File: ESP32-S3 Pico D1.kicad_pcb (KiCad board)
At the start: 6 copper layers, 31 x 30.5 mm, 88 parts, among them CN1 GT-USB-7014D, CN2 BM04B-ACHSS, CN3 2337019-1, SW1 SPST-NO, SW2 SPST-NO, U1 SKYA21024, U11 74LVC1G38, U12 74LVC1G38, U13 74LVC1G38, U2 TPS2121, U3 TPS2121, U4 TPSM82903, U5 TPSM82903, U6 ESP32-S3-PICO-1-N8R2, U8 TCAN1057AVDRBRQ1, U9 TS3USB221A-Q1

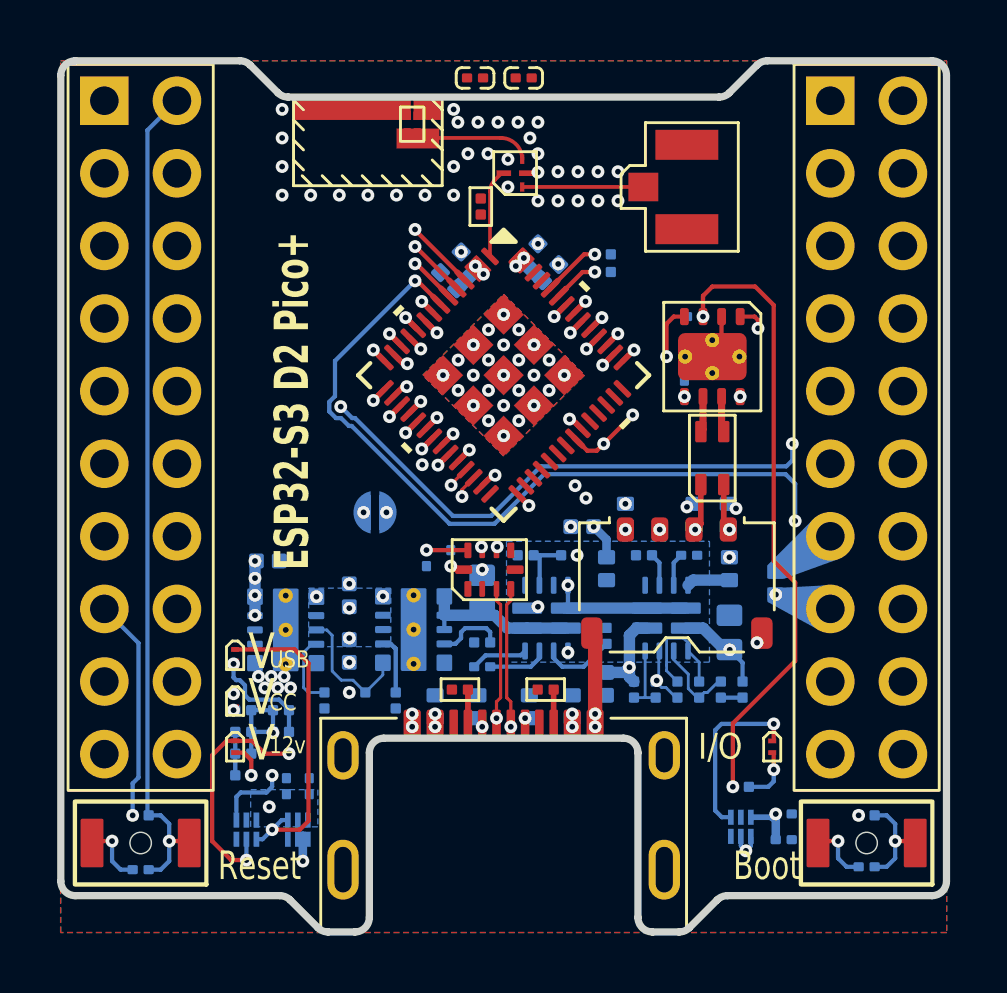
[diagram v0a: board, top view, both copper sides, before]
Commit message: streamlined routing by discarding legacy GPIO pinout compatibility. reduced Vin to Vcc and Vbus (no more +16V) includes CAN & Vehicle inputs (need to move to 2nd board, though) added wake-on-start by wiring Vacc to RTC_IO
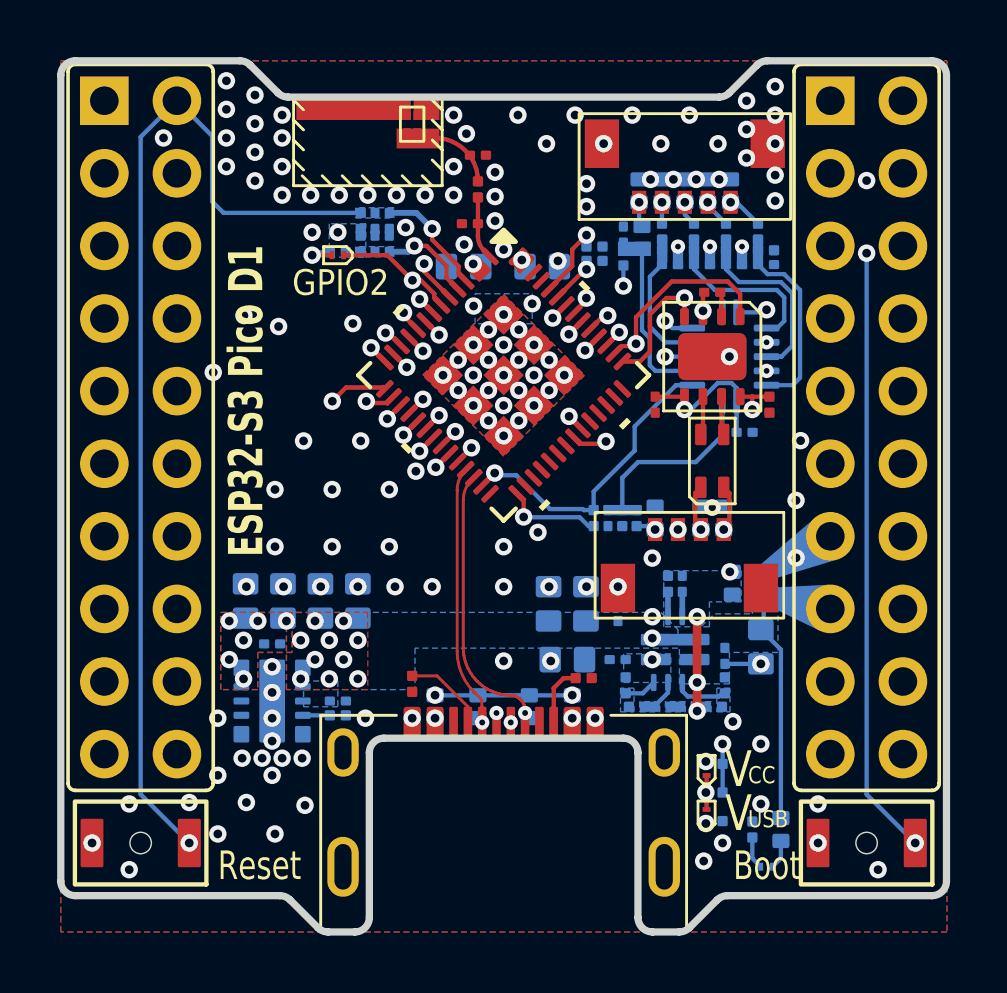
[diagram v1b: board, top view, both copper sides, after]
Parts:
- removed JP1: SolderJumper_2_Open, Personal_FootprintLibrary:SolderJumper-2_Open
- removed R22: 1k, Resistors:R0201_Dense
- removed U11, U12, U13: 74LVC1G38, Personal_FootprintLibrary:DSF6
- removed U6: ESP32-S3-PICO-1-N8R2, Personal_FootprintLibrary:ESP32-S3-Pico-1
- removed U8: TCAN1057AVDRBRQ1, Personal_FootprintLibrary:VSON-8-1EP_3x3mm_P0.65mm_EP1.65x2.4mm_ThermalVias
- removed U9: TS3USB221A-Q1, Personal_FootprintLibrary:Texas_UQFN-10_1.5x2mm_P0.5mm
- added C13: 47uF, Capacitors:C_0603_Dense, B.Cu at (142.3, 118.9)
- added C27: 1uF, Capacitors:C_0201_Dense, B.Cu at (159.2, 107.1)
- added C30: 1uF, Capacitors:C_0201_Dense, B.Cu at (155.8, 107.1)
- added C31: 1uF, Capacitors:C_0201_Dense, B.Cu at (153.7, 116.0)
- added C32: 1uF, Capacitors:C_0201_Dense, B.Cu at (154.2, 106.1)
- added C7: 1uF, Capacitors:C_0201_Dense, B.Cu at (144.2, 122.4)
- added D11: D15V0H1U2LP-7B, Personal_FootprintLibrary:DFN1006-2, B.Cu at (157.9, 104.5)
- added D12: D15V0H1U2LP-7B, Personal_FootprintLibrary:DFN1006-2, B.Cu at (157.1, 104.5)
- added D13: D15V0H1U2LP-7B, Personal_FootprintLibrary:DFN1006-2, B.Cu at (156.3, 104.5)
- added D14: D15V0H1U2LP-7B, Personal_FootprintLibrary:DFN1006-2, B.Cu at (155.5, 104.5)
- added D15: D15V0H1U2LP-7B, Personal_FootprintLibrary:DFN1006-2, B.Cu at (154.7, 104.5)
- added D16: D15V0H1U2LP-7B, Personal_FootprintLibrary:DFN1006-2, B.Cu at (154.8, 106.2)
- added R25: 10k, Resistors:R_0201_Dense, B.Cu at (159.2, 106.6)
- added R29: 10k, Resistors:R_0201_Dense, B.Cu at (156.9, 106.6)
- added R31: 10k, Resistors:R_0201_Dense, B.Cu at (155.8, 106.6)
- added R32: 26k1, Resistors:R_0201_Dense, B.Cu at (154.2, 116.0)
- added R33: 10k, Resistors:R_0201_Dense, B.Cu at (153.2, 116.0)
- added R35: 10k, Resistors:R_0201_Dense, B.Cu at (154.2, 106.9)
- C1: value 22uF -> 47uF; footprint Capacitors:C0603_Dense -> Capacitors:C_0603_Dense
- C10, C12, C19, C2, C20, C21, C3: value 22uF -> 1uF; footprint Capacitors:C0402_Dense -> Capacitors:C_0201_Dense
- C11: value 22uF -> 47uF; footprint Capacitors:C0402_Dense -> Capacitors:C_0603_Dense
- C14, C23, C4, C5, C8, C9: value 1uF -> 47uF; footprint Capacitors:C0201_Dense -> Capacitors:C_0603_Dense
- C15, C16: value 1uF -> DNP; footprint Capacitors:C0201_Dense -> Capacitors:C_0201_Dense; moved to F.Cu
- C17: value 22uF -> 1uF; footprint Capacitors:C0402_Dense -> Capacitors:C_0201_Dense; moved to F.Cu
- C18: value 22uF -> 1uF; footprint Capacitors:C0603_Dense -> Capacitors:C_0201_Dense; moved to F.Cu
- C22: value 100nF -> 1uF; footprint Capacitors:C0201_Dense -> Capacitors:C_0201_Dense
- C24: value 100nF -> 47uF; footprint Capacitors:C0201_Dense -> Capacitors:C_0603_Dense
- C26, C6: footprint Capacitors:C0201_Dense -> Capacitors:C_0201_Dense
- C28, C29: value DNP -> 1uF; footprint Capacitors:C0201_Dense -> Capacitors:C_0201_Dense; moved to B.Cu
- CN2: value BM04B-ACHSS -> SM04B-SURS-TF(LF)(SN); footprint Personal_FootprintLibrary:JST_ACH_BM04B-ACHSS-A-GAN-ETF_1x04-1MP_P1.20mm_Vertical -> Personal_FootprintLibrary:JST_SUH_1x04_MP_P0.8mm
- CN3: value 2337019-1 -> SM05B-SURS-TF(LF)(SN); footprint Personal_FootprintLibrary:u.FL_Male_Pin_Coax_SMD -> Personal_FootprintLibrary:JST_SUH_1x05_MP_P0.8mm
- D2: value ESDSLC24VLB-TP -> D15V0H1U2LP-7B
- D3, D7, D8: value ESDSLC24VLB-TP -> SZESD7241N2T5G
- D4: value D15V0H1U2LP-7B -> SZESD7241N2T5G
- H1, H2: footprint Personal_FootprintLibrary:PinHeader_2x10_P2.54mm_Vertical -> Personal_FootprintLibrary:PinHeader_2x10_P2.54mm_Vertical_BottomMount_TopReference
- LED2: value Green -> Orange
- LED3: value Orange -> Green
- LED4: moved to B.Cu
- R1: value 40k2 -> 5k1; footprint Resistors:R0201_Dense -> Resistors:R_0201_Dense; moved to F.Cu
- R10: value 1k -> 5k1; footprint Resistors:R0201_Dense -> Resistors:R_0201_Dense
- R11: value 1k -> 0R; footprint Resistors:R0201_Dense -> Resistors:R_0201_Dense; moved to F.Cu
- R12, R13, R19, R23: footprint Resistors:R0201_Dense -> Resistors:R_0201_Dense
- R14, R16, R17: value 95k3 -> 5k1; footprint Resistors:R0201_Dense -> Resistors:R_0201_Dense
- R15, R9: value 40k2 -> 5k1; footprint Resistors:R0201_Dense -> Resistors:R_0201_Dense
- R18: value 40k2 -> 1k; footprint Resistors:R0201_Dense -> Resistors:R_0201_Dense
- R2: value 95k3 -> 5k1; footprint Resistors:R0201_Dense -> Resistors:R_0201_Dense; moved to F.Cu
- R20: footprint Resistors:R0201_Dense -> Resistors:R_0201_Dense; moved to F.Cu
- R21, R4, R7: value 95k3 -> 76k8; footprint Resistors:R0201_Dense -> Resistors:R_0201_Dense
- R24: value 1k -> 47k; footprint Resistors:R0201_Dense -> Resistors:R_0201_Dense
- R26: value 95k3 -> 47k; footprint Resistors:R0201_Dense -> Resistors:R_0201_Dense
- R27: value 40k2 -> 10k; footprint Resistors:R0201_Dense -> Resistors:R_0201_Dense
- R28: value 40k2 -> 47k; footprint Resistors:R0201_Dense -> Resistors:R_0201_Dense
- R3: value 40k2 -> 76k8; footprint Resistors:R0201_Dense -> Resistors:R_0201_Dense
- R30: value 0R -> 47k; footprint Resistors:R0201_Dense -> Resistors:R_0201_Dense; moved to B.Cu
- R5: value 5k1 -> 26k1; footprint Resistors:R0201_Dense -> Resistors:R_0201_Dense; moved to B.Cu
- R6: value 5k1 -> 76k8; footprint Resistors:R0201_Dense -> Resistors:R_0201_Dense; moved to B.Cu
- R8: value 1k -> 26k1; footprint Resistors:R0201_Dense -> Resistors:R_0201_Dense
- U1: value SKYA21024 -> TPS2121; footprint Personal_FootprintLibrary:SKYA21024 -> Personal_FootprintLibrary:VQHN-HR-12; moved to B.Cu
- U2: value TPS2121 -> TPSM82903; footprint Personal_FootprintLibrary:VQHN-HR-12 -> Personal_FootprintLibrary:uSIP-11_3.0x2.8
- U3: value TPS2121 -> ESP32-S3-PICO-1-N8R2; footprint Personal_FootprintLibrary:VQHN-HR-12 -> Personal_FootprintLibrary:ESP32-S3-Pico-1; moved to F.Cu
- U4: value TPSM82903 -> TCAN1057AVDRBRQ1; footprint Personal_FootprintLibrary:uSIP-11_3.0x2.8_ThermalVias -> Personal_FootprintLibrary:VSON-8-1EP_3x3mm_P0.65mm_EP1.65x2.4mm; moved to F.Cu
- U5: value TPSM82903 -> 74LVC06A; footprint Personal_FootprintLibrary:uSIP-11_3.0x2.8_ThermalVias -> Personal_FootprintLibrary:DHVQFN-14-1EP_2.5x3mm_P0.5mm_EP1x1.5mm
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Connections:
- ANT1 pad 1: /ESP32-S3-PICO-1/RF2 -> /ESP32-S3-PICO-1/RF_Feed
- ANT1 pad 4: /ESP32-S3-PICO-1/RF2 -> /ESP32-S3-PICO-1/RF_Feed
- C1 pad 1: 2121b -> +VBus
- C11 pad 1: +3V3 -> +5VF
- C12 pad 1: +3V3 -> +5Vext
- C15 pad 1: OV1a -> /ESP32-S3-PICO-1/RF_In
- C16 pad 1: /USB_Power_Interface/SSa -> /ESP32-S3-PICO-1/RF_Feed
- C16 pad 2: /USB_Power_Interface/GND1 -> GND
- C17 pad 1: +3V3 -> +5VF
- C18 pad 1: +16V -> +3V3
- C19 pad 1: +3V3 -> EN
- C2 pad 1: +5V1 -> +VBus
- C20 pad 1: +5Vext -> EN
- C21 pad 1: +VBus -> IO_00
- C22 pad 1: +3V3 -> IO_00
- C28 pad 1: /ESP32-S3-PICO-1/RF_In -> /CAN_Interface/Brake_F
- C29 pad 1: /ESP32-S3-PICO-1/RFC -> /CAN_Interface/Right_F
- C3 pad 1: +5V1 -> /USB_Power_Interface/SS
- C3 pad 2: GND -> GND1
- C4 pad 1: +5V1 -> +5Vext
- C5 pad 1: +3V3 -> +5VF
- C6 pad 1: /USB_Power_Interface/SSb -> +5VF
- C6 pad 2: /USB_Power_Interface/GND1 -> GND
- C8 pad 1: EN -> +5VF
- C9 pad 1: IO_00 -> +5VF
- CN2 pad 1: +16V -> /CAN_Interface/Vacc
- CN3 pad 1: /ESP32-S3-PICO-1/RF1 -> /CAN_Interface/Reverse
- CN3 pad 2: GND -> /CAN_Interface/Brake
- D10 pad 1: +VBus -> +5Vext
- D10 pad 2: GND -> /User Interface/LED4_L
- D2 pad 1: USB_D+ -> +VBus
- D3 pad 1: USB_D- -> USB_D+
- D4 pad 1: GND -> USB_D-
- D4 pad 2: /USB_Power_Interface/GND1 -> GND
- D6 pad 2: /USB_Power_Interface/GND1 -> GND1
- D9 pad 1: +16V -> /CAN_Interface/Vacc
- H1 pad 10: IO_10 -> IO_11
- H1 pad 17: IO_11 -> IO_13
- H1 pad 19: IO_13 -> IO_12
- H1 pad 20: IO_12 -> IO_10
- H1 pad 9: +5V1 -> +5VF
- H2 pad 1: unconnected-(H2-Pin_1-Pad1) -> IO_46
- H2 pad 16: IO_47 -> CAN_Silent
- H2 pad 19: IO_14 -> IO_21
- H2 pad 2: CAN_Silent -> IO_45
- H2 pad 9: IO_21 -> IO_14
- LED1 pad 1: /User Interface/LED1_L -> IO_02
- LED1 pad 2: /User Interface/LED1_H -> /User Interface/LED2_H
- LED2 pad 1: /User Interface/LED2_L -> ST
- LED2 pad 2: /User Interface/LED2_H -> /User Interface/LED1_H
- LED3 pad 2: /User Interface/LED3_H -> ST
- LED4 pad 1: STb -> /User Interface/LED4_L
- R1 pad 2: /USB_Power_Interface/SCONFc -> /USB_Power_Interface/CC2
- R10 pad 1: /User Interface/LED3_H -> GND1
- R10 pad 2: +5V1 -> /USB_Power_Interface/OV2
- R11 pad 1: /User Interface/LED4_SR -> /ESP32-S3-PICO-1/RF_In
- R11 pad 2: +5V1 -> /ESP32-S3-PICO-1/RF_Feed
- R12 pad 1: IO_00 -> GND
- R12 pad 2: +3V3 -> IO_46
- R13 pad 1: EN -> GND
- R13 pad 2: +3V3 -> IO_45
- R14 pad 1: GND -> ST
- R14 pad 2: CAN_Silent -> +3V3
- R15 pad 1: /USB_Power_Interface/GND1 -> /User Interface/LED1_H
- R15 pad 2: /USB_Power_Interface/ILMa -> +3V3
- R16 pad 1: +VBus -> EN
- R16 pad 2: /USB_Power_Interface/PR1a -> +3V3
- R17 pad 1: /USB_Power_Interface/PR1a -> IO_00
- R17 pad 2: OV1a -> +3V3
- R18 pad 1: Net-(R18-Pad1) -> /User Interface/LED2_H
- R18 pad 2: +16V -> +3V3
- R19 pad 1: /USB_Power_Interface/OV2a -> GND
- R19 pad 2: Net-(R18-Pad1) -> /User Interface/LED3_L
- R2 pad 1: /USB_Power_Interface/VSETc -> GND
- R2 pad 2: GND -> /USB_Power_Interface/CC1
- R20 pad 1: /USB_Power_Interface/GND1 -> GND
- R20 pad 2: /USB_Power_Interface/OV2a -> CAN_Silent
- R21 pad 1: OV1a -> /CAN_Interface/VaccF
- R21 pad 2: /USB_Power_Interface/GND1 -> /CAN_Interface/Vacc
- R23 pad 1: /User Interface/LED2_H -> GND
- R23 pad 2: +5V1 -> /User Interface/LED4_H
- R24 pad 1: /User Interface/LED4_H -> /CAN_Interface/Rev_F
- R24 pad 2: /User Interface/LED4_SR -> /CAN_Interface/Reverse
- R26 pad 1: +5Vext -> /CAN_Interface/Brake_F
- R26 pad 2: /USB_Power_Interface/OV2b -> /CAN_Interface/Brake
- R27 pad 1: /USB_Power_Interface/GND1 -> GND
- R27 pad 2: /USB_Power_Interface/ILMb -> /CAN_Interface/Brake_F
- R28 pad 1: /USB_Power_Interface/GND1 -> /CAN_Interface/Right_F
- R28 pad 2: /USB_Power_Interface/OV2b -> /CAN_Interface/R_Turn
- R3 pad 1: GND -> +VBus
- R3 pad 2: /USB_Power_Interface/SCONFd -> /USB_Power_Interface/PR1
- R30 pad 1: /ESP32-S3-PICO-1/RF_In -> /CAN_Interface/Left_F
- R30 pad 2: /ESP32-S3-PICO-1/RFC -> /CAN_Interface/L_Turn
- R4 pad 1: +5V1 -> /USB_Power_Interface/PR1
- R4 pad 2: /USB_Power_Interface/PG_EN -> /USB_Power_Interface/OV1
- R5 pad 1: GND -> GND1
- R5 pad 2: /USB_Power_Interface/CC2 -> /USB_Power_Interface/OV1_x
- R6 pad 1: GND -> +5Vext
- R6 pad 2: /USB_Power_Interface/CC1 -> /USB_Power_Interface/OV2
- R7 pad 1: GND -> /USB_Power_Interface/ILM
- R7 pad 2: /ESP32-S3-PICO-1/Ant_Select -> GND1
- R8 pad 1: /User Interface/LED1_H -> GND
- R8 pad 2: +5V1 -> /USB_Power_Interface/SCONFd
- R9 pad 1: /User Interface/LED2_H -> /USB_Power_Interface/OV1_x
- R9 pad 2: +5V1 -> /USB_Power_Interface/OV1
- U1 pad 1: +3V3 -> +5VF
- U1 pad 2: /ESP32-S3-PICO-1/RF1 -> +5Vext
- U1 pad 3: GND -> GND1
- U1 pad 4: /ESP32-S3-PICO-1/RF2 -> /USB_Power_Interface/OV2
- U1 pad 5: /ESP32-S3-PICO-1/Ant_Select -> /USB_Power_Interface/OV1
- U1 pad 6: /ESP32-S3-PICO-1/RFC -> /USB_Power_Interface/PR1
- U2 pad 1: 2121a -> +5VF
- U2 pad 10: /USB_Power_Interface/ILMa -> +3V3
- U2 pad 11: /USB_Power_Interface/SSa -> GND
- U2 pad 2: +16V -> +5VF
- U2 pad 3: /USB_Power_Interface/GND1 -> +5VF
- U2 pad 4: /USB_Power_Interface/OV2a -> /USB_Power_Interface/SCONFd
- U2 pad 5: OV1a -> unconnected-(U2-SS/TR-Pad5)
- U2 pad 6: /USB_Power_Interface/PR1a -> GND
- U2 pad 7: +VBus -> unconnected-(U2-FB/VSET-Pad7)
- U2 pad 8: 2121a -> unconnected-(U2-SW-Pad8)
- U2 pad 9: /USB_Power_Interface/GND1 -> +3V3
- U3 pad 1: 2121b -> /ESP32-S3-PICO-1/RF_In
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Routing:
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- added copper zone on F.Cu, net +3V3
- added copper zone on In2.Cu, net +3V3
- added copper zone on B.Cu, net +5VF
- added copper zone on F.Cu, net +5VF
- added copper zone on In1.Cu, net +5VF
- added copper zone on In2.Cu, net +5VF
- added copper zone on In3.Cu, net +5VF
- added copper zone on B.Cu, net +5Vext
- added copper zone on B.Cu, net +VBus
- added copper zone on In4.Cu, net +VBus
- added copper zone on B.Cu, net /USB_Power_Interface/OV1
- added copper zone on B.Cu, net /USB_Power_Interface/OV1_x
- added copper zone on B.Cu, net /USB_Power_Interface/OV2
- added copper zone on B.Cu, net /USB_Power_Interface/PR1
- added copper zone on B.Cu, net EN
- added copper zone on B.Cu, net GND1
- added copper zone on B.Cu, net IO_00
- removed copper zone on B.Cu, net +5V1
- removed copper zone on In4.Cu, net +5V1
- removed copper zone on B.Cu, net /USB_Power_Interface/GND1
- removed copper zone on In1.Cu, net /USB_Power_Interface/GND1
- removed copper zone on In2.Cu, net /USB_Power_Interface/GND1
- removed copper zone on In3.Cu, net /USB_Power_Interface/GND1
- removed copper zone on In4.Cu, net /USB_Power_Interface/GND1
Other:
- board text added: "ESP32-S3 Pico D1"
- board text added: "GPIO2"
- board text added: "Polarity!"
- board text added: "RHK ESP32-S3 D2 Pico"
- board text added: "Reverse"
- board text removed: "12v"
- board text removed: "ESP32-S3 D2 Pico+"
- board text removed: "I/O"
- board text removed: "RHK ESP32-S3 D2 Pico+"

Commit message: Update .gitignore, BOM-ESP32-S3 Pico D1.csv, CANBus_Interface.kicad_sch, and 14 more files
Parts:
- removed CN2: SM04B-SURS-TF(LF)(SN), Personal_FootprintLibrary:JST_SUH_1x04_MP_P0.8mm
- removed CN3: SM05B-SURS-TF(LF)(SN), Personal_FootprintLibrary:JST_SUH_1x05_MP_P0.8mm
- removed R23: 5k1, Resistors:R_0201_Dense
- added J**: BM20BNSHDZSTFT, 000JST:BM20BNSHDZSTFT, F.Cu at (145.6, 80.3)
- added J**: BM20BNSHDZSTFT, 000JST:BM20BNSHDZSTFT, F.Cu at (154.4, 80.3)
- added J**: SM10B-NSHSS-TB-LFSN, 000JST:SM10B-NSHSS-TB-LFSN, F.Cu at (150.0, 94.3)
- added OSC1: 40MHz, Personal_FootprintLibrary:SIT8XXXxx-7Y-xxx, F.Cu at (175.1, 120.8)
- added R22: 5k1, Resistors:R_0201_Dense, B.Cu at (157.4, 126.6)
- added REF**: SAMTEC_HLE-110-02-L-DV-BE-K-TR, Personal_FootprintLibrary:PinHeader_2x10_P2.54mm_LowProfile_BottomEntrySMD, F.Cu at (137.3, 86.0)
- added REF**: SAMTEC_HLE-110-02-L-DV-BE-K-TR, Personal_FootprintLibrary:PinHeader_2x10_P2.54mm_LowProfile_BottomEntrySMD, F.Cu at (-1337.3, 112.8)
- added REF**: SAMTEC_HLE-110-02-L-DV-BE-K-TR, Personal_FootprintLibrary:PinHeader_2x10_P2.54mm_LowProfile_BottomEntrySMD, F.Cu at (-1362.7, 112.8)
- added REF**: SAMTEC_HLE-110-02-L-DV-BE-K-TR, Personal_FootprintLibrary:PinHeader_2x10_P2.54mm_LowProfile_BottomEntrySMD, F.Cu at (162.7, 86.0)
- C10, C2: value 1uF -> 47uF; footprint Capacitors:C_0201_Dense -> Capacitors:C_0603_Dense
- C13, C24: value 47uF -> 1uF; footprint Capacitors:C_0603_Dense -> Capacitors:C_0201_Dense
- C15: value DNP -> 47uF; footprint Capacitors:C_0201_Dense -> Capacitors:C_0603_Dense; moved to B.Cu
- C16: value DNP -> 1uF; moved to B.Cu
- C3: value 1uF -> DNP; moved to F.Cu
- C4: value 47uF -> DNP; footprint Capacitors:C_0603_Dense -> Capacitors:C_0201_Dense; moved to F.Cu
- LED1: value Blue -> Orange
- LED2: value Orange -> Red; moved to B.Cu
- LED3: value Green -> Blue
- LED4: value Red -> Green; moved to F.Cu
- R1: value 5k1 -> 0R
- R10: value 5k1 -> 76k8
- R11: value 0R -> 76k8; moved to B.Cu
- R12, R9: value 5k1 -> 26k1
- R2: moved to B.Cu
- R3: value 76k8 -> 5k1
- R4: value 76k8 -> 5k1; moved to F.Cu
- R5: value 26k1 -> 5k1; moved to F.Cu
- R8: value 26k1 -> 5k1
- U1: value TPS2121 -> ESP32-S3-PICO-1-N8R2; footprint Personal_FootprintLibrary:VQHN-HR-12 -> Personal_FootprintLibrary:ESP32-S3-Pico-1; moved to F.Cu
- U2: value TPSM82903 -> TPS2121; footprint Personal_FootprintLibrary:uSIP-11_3.0x2.8 -> Personal_FootprintLibrary:VQHN-HR-12
- U3: value ESP32-S3-PICO-1-N8R2 -> TPSM82903; footprint Personal_FootprintLibrary:ESP32-S3-Pico-1 -> Personal_FootprintLibrary:uSIP-11_3.0x2.8; moved to B.Cu
- moved C30 48.2 mm to (203.6, 113.7)
- moved D12 48.2 mm to (204.9, 111.2)
- moved D14 48.2 mm to (203.3, 111.2)
- moved R30 48.2 mm to (203.3, 112.6)
- moved R31 48.2 mm to (203.6, 113.2)
- moved C26 48.2 mm to (206.2, 119.6)
- moved C27 48.2 mm to (206.9, 113.7)
- moved C28 48.2 mm to (205.8, 113.7)
- moved C29 48.2 mm to (204.7, 113.7)
- moved C31 48.2 mm to (201.4, 122.6)
- moved C32 48.2 mm to (201.9, 112.7)
- moved D11 48.2 mm to (205.7, 111.2)
- moved D13 48.2 mm to (204.1, 111.2)
- moved D15 48.2 mm to (202.5, 111.2)
- moved D16 48.2 mm to (202.6, 112.8)
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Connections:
- net /CAN_Interface/Brake renamed /IO_Board/GR86 Inputs/Brake
- net /CAN_Interface/Brake_F renamed /IO_Board/GR86 Inputs/Brake_F
- net /CAN_Interface/CAN_F_N renamed /IO_Board/CAN Bus/CAN_F_N
- net /CAN_Interface/CAN_F_P renamed /IO_Board/CAN Bus/CAN_F_P
- net /CAN_Interface/CAN_N renamed /IO_Board/CAN Bus/CAN_N
- net /CAN_Interface/CAN_P renamed /IO_Board/CAN Bus/CAN_P
- net /CAN_Interface/Dome renamed /IO_Board/GR86 Inputs/Dome
- net /CAN_Interface/L_Turn renamed /IO_Board/GR86 Inputs/LTurn
- net /CAN_Interface/Left_F renamed /IO_Board/GR86 Inputs/LTurn_F
- net /CAN_Interface/R_Turn renamed /IO_Board/GR86 Inputs/RTurn
- net /CAN_Interface/Rev_F renamed /IO_Board/GR86 Inputs/Rev_F
- net /CAN_Interface/Reverse renamed /IO_Board/GR86 Inputs/Reverse
- net /CAN_Interface/Right_F renamed /IO_Board/GR86 Inputs/RTurn_F
- net /CAN_Interface/VaccF renamed /IO_Board/GR86 Inputs/VaccF
- net /CAN_Interface/~{BRAKE} renamed /IO_Board/GR86 Inputs/~{Brake}
- net /CAN_Interface/~{Dome_F} renamed /IO_Board/GR86 Inputs/~{Dome_F}
- net /CAN_Interface/~{Dome} renamed /IO_Board/GR86 Inputs/~{Dome}
- net /CAN_Interface/~{LTURN} renamed /IO_Board/GR86 Inputs/~{LTurn}
- net /CAN_Interface/~{REV} renamed /IO_Board/GR86 Inputs/~{Reverse}
- net /CAN_Interface/~{RTURN} renamed /IO_Board/GR86 Inputs/~{RTurn}
- ANT1 pad 1: /ESP32-S3-PICO-1/RF_Feed -> /ESP32-S3 Board/ESP32-S3-PICO-1/RF_Feed
- ANT1 pad 4: /ESP32-S3-PICO-1/RF_Feed -> /ESP32-S3 Board/ESP32-S3-PICO-1/RF_Feed
- C1 pad 1: +VBus -> +3V3
- C10 pad 1: +3V3 -> +5VF
- C12 pad 1: +5Vext -> +5VF
- C15 pad 1: /ESP32-S3-PICO-1/RF_In -> +3V3
- C16 pad 1: /ESP32-S3-PICO-1/RF_Feed -> /ESP32-S3 Board/USB_Power_Interface/SS
- C16 pad 2: GND -> GND1
- C2 pad 1: +VBus -> +3V3
- C23 pad 1: +3V3 -> +5Vext
- C24 pad 1: +3V3 -> +5Vext
- C3 pad 1: /USB_Power_Interface/SS -> /ESP32-S3 Board/ESP32-S3-PICO-1/RF_In
- C3 pad 2: GND1 -> GND
- C4 pad 1: +5Vext -> /ESP32-S3 Board/ESP32-S3-PICO-1/RF_Feed
- C5 pad 1: +5VF -> +VBus
- C6 pad 1: +5VF -> +VBus
- CN1 pad A5: /USB_Power_Interface/CC1 -> /ESP32-S3 Board/USB_Power_Interface/CC1
- CN1 pad A6: USB_D+ -> /ESP32-S3 Board/ESP32-S3-PICO-1/USB_D+
- CN1 pad A7: USB_D- -> /ESP32-S3 Board/ESP32-S3-PICO-1/USB_D-
- CN1 pad B5: /USB_Power_Interface/CC2 -> /ESP32-S3 Board/USB_Power_Interface/CC2
- CN1 pad B6: USB_D+ -> /ESP32-S3 Board/ESP32-S3-PICO-1/USB_D+
- CN1 pad B7: USB_D- -> /ESP32-S3 Board/ESP32-S3-PICO-1/USB_D-
- D10 pad 2: /User Interface/LED4_L -> /ESP32-S3 Board/User Interface/LED4_L
- D3 pad 1: USB_D+ -> /ESP32-S3 Board/ESP32-S3-PICO-1/USB_D+
- D4 pad 1: USB_D- -> /ESP32-S3 Board/ESP32-S3-PICO-1/USB_D-
- D9 pad 1: /CAN_Interface/Vacc -> /IO_Board/CAN Bus/Vacc
- H1 pad 10: IO_11 -> IO_04
- H1 pad 15: IO_07 -> IO_09
- H1 pad 16: IO_06 -> IO_11
- H1 pad 19: IO_12 -> IO_08
- H1 pad 20: IO_10 -> IO_06
- H1 pad 5: IO_04 -> IO_07
- H1 pad 6: IO_09 -> IO_10
- H1 pad 7: IO_08 -> IO_12
- H2 pad 11: GND -> RELAY_GND
- H2 pad 16: CAN_Silent -> IO_48
- H2 pad 17: IO_48 -> IO_16
- H2 pad 6: IO_16 -> IO_47
- LED1 pad 1: IO_02 -> ST
- LED1 pad 2: /User Interface/LED2_H -> /ESP32-S3 Board/User Interface/LED1_H
- LED2 pad 1: ST -> /ESP32-S3 Board/User Interface/LED4_L
- LED2 pad 2: /User Interface/LED1_H -> /ESP32-S3 Board/User Interface/LED4_H
- LED3 pad 1: /User Interface/LED3_L -> IO_02
- LED3 pad 2: ST -> /ESP32-S3 Board/User Interface/LED2_H
- LED4 pad 1: /User Interface/LED4_L -> /ESP32-S3 Board/User Interface/LED3_L
- LED4 pad 2: /User Interface/LED4_H -> ST
- R1 pad 1: GND -> /ESP32-S3 Board/ESP32-S3-PICO-1/RF_In
- R1 pad 2: /USB_Power_Interface/CC2 -> /ESP32-S3 Board/ESP32-S3-PICO-1/RF_Feed
- R10 pad 1: GND1 -> +5Vext
- R10 pad 2: /USB_Power_Interface/OV2 -> /ESP32-S3 Board/USB_Power_Interface/OV2
- R11 pad 1: /ESP32-S3-PICO-1/RF_In -> /ESP32-S3 Board/USB_Power_Interface/ILM
- R11 pad 2: /ESP32-S3-PICO-1/RF_Feed -> GND1
- R12 pad 2: IO_46 -> /ESP32-S3 Board/USB_Power_Interface/SCONFd
- R13 pad 1: GND -> GND1
- R13 pad 2: IO_45 -> /ESP32-S3 Board/USB_Power_Interface/OV2
- R15 pad 1: /User Interface/LED1_H -> /ESP32-S3 Board/User Interface/LED1_H
- R18 pad 1: /User Interface/LED2_H -> /ESP32-S3 Board/User Interface/LED2_H
- R19 pad 2: /User Interface/LED3_L -> /ESP32-S3 Board/User Interface/LED4_H
- R2 pad 2: /USB_Power_Interface/CC1 -> IO_46
- R20 pad 2: CAN_Silent -> /IO_Board/CAN Bus/CAN Silent Mode Select
- R21 pad 2: /CAN_Interface/Vacc -> /IO_Board/GR86 Inputs/Vacc
- R3 pad 1: +VBus -> GND
- R3 pad 2: /USB_Power_Interface/PR1 -> IO_45
- R33 pad 1: IO_21 -> /IO_Board/GR86 Inputs/~{WakeOnStart}
- R4 pad 1: /USB_Power_Interface/PR1 -> GND
- R4 pad 2: /USB_Power_Interface/OV1 -> /ESP32-S3 Board/USB_Power_Interface/CC2
- R5 pad 1: GND1 -> GND
- R5 pad 2: /USB_Power_Interface/OV1_x -> /ESP32-S3 Board/USB_Power_Interface/CC1
- R6 pad 1: +5Vext -> +VBus
- R6 pad 2: /USB_Power_Interface/OV2 -> /ESP32-S3 Board/USB_Power_Interface/PR1
- R7 pad 1: /USB_Power_Interface/ILM -> /ESP32-S3 Board/USB_Power_Interface/PR1
- R7 pad 2: GND1 -> /ESP32-S3 Board/USB_Power_Interface/OV1
- R8 pad 1: GND -> /ESP32-S3 Board/USB_Power_Interface/OV1_x
- R8 pad 2: /USB_Power_Interface/SCONFd -> /ESP32-S3 Board/USB_Power_Interface/OV1
- R9 pad 1: /USB_Power_Interface/OV1_x -> GND1
- R9 pad 2: /USB_Power_Interface/OV1 -> /ESP32-S3 Board/USB_Power_Interface/OV1_x
- U1 pad 1: +5VF -> /ESP32-S3 Board/ESP32-S3-PICO-1/RF_In
- U1 pad 10: /USB_Power_Interface/ILM -> IO_05
- U1 pad 11: /USB_Power_Interface/SS -> IO_06
- U1 pad 12: GND1 -> IO_07
- U1 pad 2: +5Vext -> +3V3
- U1 pad 3: GND1 -> +3V3
- U1 pad 4: /USB_Power_Interface/OV2 -> EN
- U1 pad 5: /USB_Power_Interface/OV1 -> IO_00
- U1 pad 6: /USB_Power_Interface/PR1 -> IO_01
- U1 pad 7: +VBus -> IO_02
- U1 pad 8: +5VF -> IO_03
- U1 pad 9: ST -> IO_04
- U2 pad 10: +3V3 -> /ESP32-S3 Board/USB_Power_Interface/ILM
- U2 pad 11: GND -> /ESP32-S3 Board/USB_Power_Interface/SS
- U2 pad 2: +5VF -> +5Vext
- U2 pad 3: +5VF -> GND1
- U2 pad 4: /USB_Power_Interface/SCONFd -> /ESP32-S3 Board/USB_Power_Interface/OV2
- U2 pad 5: unconnected-(U2-SS/TR-Pad5) -> /ESP32-S3 Board/USB_Power_Interface/OV1
- U2 pad 6: GND -> /ESP32-S3 Board/USB_Power_Interface/PR1
- U2 pad 7: unconnected-(U2-FB/VSET-Pad7) -> +VBus
- U2 pad 8: unconnected-(U2-SW-Pad8) -> +5VF
- U2 pad 9: +3V3 -> ST
- U3 pad 1: /ESP32-S3-PICO-1/RF_In -> +5VF
- U3 pad 10: IO_05 -> +3V3
- U3 pad 11: IO_06 -> GND
- U3 pad 2: +3V3 -> +5VF
- U3 pad 3: +3V3 -> +5VF
- U3 pad 4: EN -> /ESP32-S3 Board/USB_Power_Interface/SCONFd
- U3 pad 5: IO_00 -> unconnected-(U3-SS/TR-Pad5)
- U3 pad 6: IO_01 -> GND
- U3 pad 7: IO_02 -> unconnected-(U3-FB/VSET-Pad7)
- U3 pad 8: IO_03 -> unconnected-(U3-SW-Pad8)
- U3 pad 9: IO_04 -> +3V3
- U4 pad 1: IO_39 -> /IO_Board/CAN Bus/CAN Send Data
- U4 pad 4: IO_38 -> /IO_Board/CAN Bus/CAN Rcv Data
- U4 pad 8: CAN_Silent -> /IO_Board/CAN Bus/CAN Silent Mode Select
- U5 pad 2: IO_21 -> /IO_Board/GR86 Inputs/~{WakeOnStart}
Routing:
- net CAN_Silent: track 15.3 -> 0.00 mm, vias 2 -> 0
- net +5VF: track 29.6 -> 16.3 mm, vias 12 -> 10
- net IO_06: track 10.9 -> 23.1 mm
- net IO_11: track 20.5 -> 8.53 mm, vias 1 -> 0
- net USB_D-: track 11.3 -> 0.00 mm, vias 2 -> 0
- net /ESP32-S3 Board/ESP32-S3-PICO-1/USB_D-: track 0.00 -> 11.3 mm, vias 0 -> 2
- net IO_47: track 0.00 -> 11.0 mm, vias 0 -> 1
- net USB_D+: track 10.9 -> 0.00 mm, vias 2 -> 0
- net /ESP32-S3 Board/ESP32-S3-PICO-1/USB_D+: track 0.00 -> 10.9 mm, vias 0 -> 2
- net IO_21: track 30.7 -> 20.1 mm
- net +3V3: track 28.9 -> 18.5 mm, vias 15 -> 13
- net IO_04: track 13.9 -> 24.2 mm
- net IO_10: track 19.6 -> 10.9 mm, vias 1 -> 0
- net IO_39: track 19.5 -> 10.9 mm
- net /IO_Board/GR86 Inputs/Rev_F: track 6.74 -> 0.00 mm
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- removed copper zone on B.Cu, net /USB_Power_Interface/OV1
- removed copper zone on B.Cu, net /USB_Power_Interface/OV1_x
- removed copper zone on B.Cu, net /USB_Power_Interface/OV2
- removed copper zone on B.Cu, net /USB_Power_Interface/PR1

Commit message: Update CANBus_Interface.kicad_sch, ESP32-S3 D1 Pico Board.kicad_sch, ESP32-S3 Pico D1.kicad_pcb, and 15 more files
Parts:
- removed C10, C11, C14, C15, C2, C23, C5, C8, C9: 47uF, Capacitors:C_0603_Dense
- removed C12, C13, C16, C17, C18, C19, C20, C21, C22, C24, C26, C27, C28, C29, C30, C31, C32, C6, C7: 1uF, Capacitors:C_0201_Dense
- removed D10, D12, D13, D14, D16: D15V0H1U2LP-7B, Personal_FootprintLibrary:DFN1006-2
- removed H1, H2: ESP_Header, Personal_FootprintLibrary:PinHeader_2x10_P2.54mm_Vertical_BottomMount_TopReference
- removed J** (x2): BM20BNSHDZSTFT, 000JST:BM20BNSHDZSTFT
- removed J**: SM10B-NSHSS-TB-LFSN, 000JST:SM10B-NSHSS-TB-LFSN
- removed OSC1: 40MHz, Personal_FootprintLibrary:SIT8XXXxx-7Y-xxx
- removed R10, R11, R21, R7: 76k8, Resistors:R_0201_Dense
- removed R12, R32: 26k1, Resistors:R_0201_Dense
- removed R13, R14, R15, R16, R17, R19, R2, R20, R22, R3, R5, R8: 5k1, Resistors:R_0201_Dense
- removed R18: 1k, Resistors:R_0201_Dense
- removed R24, R26, R28, R30: 47k, Resistors:R_0201_Dense
- removed R25, R27, R29, R31, R33, R35: 10k, Resistors:R_0201_Dense
- removed REF** (x4): SAMTEC_HLE-110-02-L-DV-BE-K-TR, Personal_FootprintLibrary:PinHeader_2x10_P2.54mm_LowProfile_BottomEntrySMD
- removed U4: TCAN1057AVDRBRQ1, Personal_FootprintLibrary:VSON-8-1EP_3x3mm_P0.65mm_EP1.65x2.4mm
- removed U5: 74LVC06A, Personal_FootprintLibrary:DHVQFN-14-1EP_2.5x3mm_P0.5mm_EP1x1.5mm
- added C1001: 0.1uF, My Capacitors:C_0201_Dense, F.Cu at (135.5, 92.4)
- added C402: 22uF, My Capacitors:C_0603_Dense, B.Cu at (150.1, 115.8)
- added C403: 22uF, My Capacitors:C_0603_Dense, B.Cu at (153.3, 109.1)
- added C404: 22uF, My Capacitors:C_0603_Dense, B.Cu at (151.1, 106.0)
- added C405: 22uF, My Capacitors:C_0603_Dense, B.Cu at (146.0, 110.5)
- added C501: 22uF, My Capacitors:C_0603_Dense, B.Cu at (159.2, 119.5)
- added C502: 0.1uF, My Capacitors:C_0201_Dense, B.Cu at (158.1, 119.5)
- added C503: 22uF, My Capacitors:C_0603_Dense, B.Cu at (152.1, 119.7)
- added C504: 0.1uF, My Capacitors:C_0201_Dense, B.Cu at (153.7, 120.5)
- added C505: 0.1uF, My Capacitors:C_0201_Dense, B.Cu at (155.6, 116.9)
- added C506: 0.1uF, My Capacitors:C_0201_Dense, B.Cu at (154.2, 117.8)
- added C507: 22uF, My Capacitors:C_0603_Dense, B.Cu at (153.2, 117.5)
- added C508: 22uF, My Capacitors:C_0603_Dense, B.Cu at (151.8, 117.5)
- added C509: 22uF, My Capacitors:C_0603_Dense, B.Cu at (144.9, 117.5)
- added C510: 22uF, My Capacitors:C_0603_Dense, B.Cu at (143.6, 117.5)
- added C511: 0.1uF, My Capacitors:C_0201_Dense, B.Cu at (144.2, 120.9)
- added C512: 0.1uF, My Capacitors:C_0201_Dense, B.Cu at (141.9, 119.0)
- added C513: 22uF, My Capacitors:C_0603_Dense, B.Cu at (142.2, 117.5)
- added C514: 22uF, My Capacitors:C_0603_Dense, B.Cu at (140.9, 117.5)
- added C601: 0.1uF, My Capacitors:C_0201_Dense, B.Cu at (145.4, 104.3)
- added C701: 22uF, My Capacitors:C_0603_Dense, B.Cu at (221.4, 32.5)
- added C702: 0.1uF, My Capacitors:C_0201_Dense, B.Cu at (214.8, 29.1)
- added C703: 0.1uF, My Capacitors:C_0201_Dense, B.Cu at (214.8, 32.2)
- added C704: 22uF, My Capacitors:C_0603_Dense, B.Cu at (221.4, 30.2)
- added C705: 0.1uF, My Capacitors:C_0201_Dense, B.Cu at (214.8, 30.6)
- added C706: 22uF, My Capacitors:C_0603_Dense, B.Cu at (221.4, 27.9)
- added C707: 22uF, My Capacitors:C_0603_Dense, B.Cu at (237.7, 35.0)
- added C708: 22uF, My Capacitors:C_0603_Dense, B.Cu at (237.7, 37.3)
- added C709: 22uF, My Capacitors:C_0603_Dense, B.Cu at (237.7, 39.6)
- added C710: 22uF, My Capacitors:C_0603_Dense, B.Cu at (237.7, 41.9)
- added C711: 10pF, My Capacitors:C_0201_Dense, B.Cu at (216.7, 27.5)
- added C712: 10pF, My Capacitors:C_0201_Dense, B.Cu at (216.7, 29.1)
- added C713: 0.1uF, My Capacitors:C_0201_Dense, B.Cu at (216.7, 30.6)
- added C714: 0.1uF, My Capacitors:C_0201_Dense, B.Cu at (216.7, 32.2)
- added C715: 0.1uF, My Capacitors:C_0201_Dense, B.Cu at (216.7, 33.7)
- added C716: 0.1uF, My Capacitors:C_0201_Dense, B.Cu at (216.7, 35.3)
- added C801: 0.1uF, My Capacitors:C_0201_Dense, B.Cu at (176.9, 89.0)
- added C802: 0.1uF, My Capacitors:C_0201_Dense, B.Cu at (99.5, 99.5)
- added C803: 0.1uF, My Capacitors:C_0201_Dense, B.Cu at (99.5, 101.1)
- added C804: 0.1uF, My Capacitors:C_0201_Dense, B.Cu at (99.5, 102.6)
- added C805: 0.1uF, My Capacitors:C_0201_Dense, B.Cu at (99.5, 104.2)
- added C806: 0.1uF, My Capacitors:C_0201_Dense, B.Cu at (176.3, 89.0)
- added C807: 0.1uF, My Capacitors:C_0201_Dense, B.Cu at (132.0, 73.3)
- added C808: 0.1uF, My Capacitors:C_0201_Dense, B.Cu at (132.0, 74.8)
- added C809: 0.1uF, My Capacitors:C_0201_Dense, B.Cu at (132.0, 76.4)
- added C810: 0.1uF, My Capacitors:C_0201_Dense, B.Cu at (101.4, 102.6)
- added C901: 0.1uF, My Capacitors:C_0201_Dense, B.Cu at (147.8, 75.9)
- added C902: 0.1uF, My Capacitors:C_0201_Dense, B.Cu at (146.2, 75.9)
- added C903: 0.1uF, My Capacitors:C_0201_Dense, B.Cu at (144.8, 75.9)
- added C904: 0.1uF, My Capacitors:C_0201_Dense, B.Cu at (143.2, 75.9)
- added C905: 0.1uF, My Capacitors:C_0201_Dense, B.Cu at (141.8, 75.9)
- added C907: 0.1uF, My Capacitors:C_0201_Dense, F.Cu at (153.6, 85.1)
- added C908: 0.1uF, My Capacitors:C_0201_Dense, F.Cu at (153.9, 85.4)
- added C909: 0.1uF, My Capacitors:C_0201_Dense, F.Cu at (154.3, 85.8)
- added C910: 4.7nF, My Capacitors:C_0201_Dense, F.Cu at (153.1, 84.4)
- added C911: 0.1uF, My Capacitors:C_0201_Dense, F.Cu at (155.7, 81.4)
- added C912: 0.1uF, My Capacitors:C_0201_Dense, F.Cu at (154.2, 81.4)
- added C913: 0.1uF, My Capacitors:C_0201_Dense, F.Cu at (155.2, 81.4)
- added C914: 0.1uF, My Capacitors:C_0201_Dense, F.Cu at (154.7, 81.4)
- added C915: 4.7nF, My Capacitors:C_0201_Dense, F.Cu at (155.2, 82.7)
- added CN301: SM32B-NSHDZS-1-TF, My Connectors:JST_NSHD_SM32B-NSHD_2x16_P1.0mm_Horizontal_SMD, F.Cu at (150.0, 70.0)
- added CN302: SM32B-NSHDZS-1-TF, My Connectors:JST_NSHD_SM32B-NSHD_2x16_P1.0mm_Horizontal_SMD, F.Cu at (150.0, 90.4)
- added D1001: PMEG4002ESFYL, Personal_FootprintLibrary:DSN0603-2, B.Cu at (141.6, 85.2)
- added D1002: PMEG4002ESFYL, Personal_FootprintLibrary:DSN0603-2, F.Cu at (141.0, 85.5)
- added D601: PMEG4002ESFYL, Personal_FootprintLibrary:DSN0603-2, B.Cu at (158.7, 124.9)
- added D701: PMEG4002ESFYL, Personal_FootprintLibrary:DSN0603-2, B.Cu at (226.9, 37.6)
- added D801: PMEG4002ESFYL, Personal_FootprintLibrary:DSN0603-2, B.Cu at (179.5, 89.0)
- added D803: PMEG4002ESFYL, Personal_FootprintLibrary:DSN0603-2, B.Cu at (178.5, 89.0)
- added D804: PMEG4002ESFYL, Personal_FootprintLibrary:DSN0603-2, B.Cu at (97.8, 89.3)
- added D805: D15V0H1U2LP-7B, Personal_FootprintLibrary:DFN1006-2, B.Cu at (155.5, 92.8)
- added D806: PMEG4002ESFYL, Personal_FootprintLibrary:DSN0603-2, B.Cu at (100.2, 85.7)
- added D807: PMEG4002ESFYL, Personal_FootprintLibrary:DSN0603-2, B.Cu at (100.2, 87.5)
- added D808: D15V0H1U2LP-7B, Personal_FootprintLibrary:DFN1006-2, B.Cu at (157.5, 87.9)
- added D809: PMEG4002ESFYL, Personal_FootprintLibrary:DSN0603-2, B.Cu at (100.2, 91.2)
- added D810: PMEG4002ESFYL, Personal_FootprintLibrary:DSN0603-2, B.Cu at (102.7, 85.7)
- added D811: D15V0H1U2LP-7B, Personal_FootprintLibrary:DFN1006-2, B.Cu at (156.5, 87.9)
- added D812: PMEG4002ESFYL, Personal_FootprintLibrary:DSN0603-2, B.Cu at (102.7, 89.3)
- added D813: PMEG4002ESFYL, Personal_FootprintLibrary:DSN0603-2, B.Cu at (100.3, 109.7)
- added D901: PMEG4002ESFYL, Personal_FootprintLibrary:DSN0603-2, F.Cu at (155.0, 79.1)
- added D902: PMEG4002ESFYL, Personal_FootprintLibrary:DSN0603-2, B.Cu at (141.0, 75.4)
- added D903: PMEG4002ESFYL, Personal_FootprintLibrary:DSN0603-2, B.Cu at (142.5, 75.4)
- added D904: PMEG4002ESFYL, Personal_FootprintLibrary:DSN0603-2, F.Cu at (157.7, 74.4)
- added D905: D15V0H1U2LP-7B, Personal_FootprintLibrary:DFN1006-2, B.Cu at (140.7, 74.4)
- added D906: D15V0H1U2LP-7B, Personal_FootprintLibrary:DFN1006-2, B.Cu at (142.2, 74.4)
- added D907: D15V0H1U2LP-7B, Personal_FootprintLibrary:DFN1006-2, F.Cu at (154.2, 74.8)
- added D908: PMEG4002ESFYL, Personal_FootprintLibrary:DSN0603-2, B.Cu at (144.0, 75.4)
- added D909: PMEG4002ESFYL, Personal_FootprintLibrary:DSN0603-2, B.Cu at (145.5, 75.4)
- added D910: D15V0H1U2LP-7B, Personal_FootprintLibrary:DFN1006-2, B.Cu at (143.7, 74.4)
- added D911: D15V0H1U2LP-7B, Personal_FootprintLibrary:DFN1006-2, B.Cu at (145.2, 74.4)
- added D912: PMEG4002ESFYL, Personal_FootprintLibrary:DSN0603-2, F.Cu at (154.3, 83.8)
- added D913: PMEG4002ESFYL, Personal_FootprintLibrary:DSN0603-2, B.Cu at (147.0, 75.4)
- added D914: PMEG4002ESFYL, Personal_FootprintLibrary:DSN0603-2, B.Cu at (148.5, 75.4)
- added D915: D15V0H1U2LP-7B, Personal_FootprintLibrary:DFN1006-2, B.Cu at (146.7, 74.4)
- added D916: D15V0H1U2LP-7B, Personal_FootprintLibrary:DFN1006-2, B.Cu at (148.2, 74.4)
- added H201: ESP_Header, My Connectors:PinHeader_2x10_P2.54mm_Vertical_THT_BottomMount_TopReference, B.Cu at (137.3, 111.4)
- added H202: ESP_Header, My Connectors:PinHeader_2x10_P2.54mm_Vertical_THT_BottomMount_TopReference, B.Cu at (162.7, 111.4)
- added H301: ESP_Header, My Connectors:PinHeader_2x10_P2.54mm_Vertical_THT_BottomMount_TopReference, F.Cu at (137.3, 78.4)
- added H302: ESP_Header, My Connectors:PinHeader_2x10_P2.54mm_Vertical_THT_BottomMount_TopReference, F.Cu at (162.7, 78.4)
- added Q901: NTLJS17D0P03P8Z, My Package_Leadless:WDFN6-4_2.05x2.05mm_P0.65mm, F.Cu at (152.4, 76.5)
- added R1001: 5k1, My Resistors:R_0201_Dense, F.Cu at (140.2, 85.5)
- added R1002: 33R, My Resistors:R_0201_Dense, F.Cu at (140.5, 82.2)
- added R1003: 33R, My Resistors:R_0201_Dense, F.Cu at (143.1, 80.4)
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- renumbered ANT1 to ANT401, CN1 to CN501, D1 to D501, D2 to D502, D3 to D503, D4 to D504, D5 to D505, D7 to D702, D8 to D703, D9 to D704, D11 to D802, D15 to D814, LED3 to LED601, LED4 to LED602, LED1 to LED603, LED2 to LED604, SW1 to SW601, SW2 to SW602, U1 to U401, U2 to U501, U3 to U502
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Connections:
- net +5VF renamed +5V_{FUSED}
- net +5Vext renamed +5V_{EXT}
- net +VBus renamed +V_{BUS}
- net /IO_Board/CAN Bus/CAN_N renamed /IO_Board/CAN_N
- net /IO_Board/CAN Bus/CAN_P renamed /IO_Board/CAN_P
- net EN renamed /ESP32-S3 Board/EN/Reset
- net IO_00 renamed /ESP32-S3 Board/IO00
- net IO_02 renamed /ESP32-S3 Board/IO02
- net ST renamed /ESP32-S3 Board/USB_Power_Interface/Pwr Src Ind
- D506 pad 2: GND1 -> /ESP32-S3 Board/USB_Power_Interface/GND1
- D704 pad 1: /IO_Board/CAN Bus/Vacc -> +V_{BAT}
- D802 pad 1: /IO_Board/GR86 Inputs/Reverse -> /IO_Board/Reverse_{IN}
- D814 pad 1: /IO_Board/GR86 Inputs/~{Dome} -> /IO_Board/~{Dome_{IN}}
- R505 pad 1: GND1 -> /ESP32-S3 Board/USB_Power_Interface/GND1
- R505 pad 2: /ESP32-S3 Board/USB_Power_Interface/OV1_x -> /ESP32-S3 Board/USB_Power_Interface/OV1
- U401 pad 10: IO_05 -> /ESP32-S3 Board/IO05
- U401 pad 11: IO_06 -> /ESP32-S3 Board/IO06
- U401 pad 12: IO_07 -> /ESP32-S3 Board/IO07
- U401 pad 13: IO_08 -> /ESP32-S3 Board/IO08
- U401 pad 14: IO_09 -> /ESP32-S3 Board/ESP32-S3-PICO-1/GPIO09
- U401 pad 15: IO_10 -> /ESP32-S3 Board/IO10
- U401 pad 16: IO_11 -> /ESP32-S3 Board/ESP32-S3-PICO-1/GPIO11
- U401 pad 17: IO_12 -> /ESP32-S3 Board/ESP32-S3-PICO-1/GPIO12
- U401 pad 18: IO_13 -> /ESP32-S3 Board/ESP32-S3-PICO-1/GPIO13
- U401 pad 19: IO_14 -> /ESP32-S3 Board/ESP32-S3-PICO-1/GPIO14
- U401 pad 21: IO_15 -> /ESP32-S3 Board/IO15
- U401 pad 22: IO_16 -> /ESP32-S3 Board/IO16
- U401 pad 23: IO_17 -> /ESP32-S3 Board/IO17
- U401 pad 24: IO_18 -> /ESP32-S3 Board/IO18
- U401 pad 27: IO_21 -> /ESP32-S3 Board/IO21
- U401 pad 36: IO_48 -> /ESP32-S3 Board/IO48
- U401 pad 37: IO_47 -> /ESP32-S3 Board/IO47
- U401 pad 43: IO_38 -> /ESP32-S3 Board/IO38
- U401 pad 44: IO_39 -> /ESP32-S3 Board/IO39
- U401 pad 45: IO_40 -> /ESP32-S3 Board/IO40
- U401 pad 47: IO_41 -> /ESP32-S3 Board/IO41
- U401 pad 48: IO_42 -> /ESP32-S3 Board/IO42
- U401 pad 49: IO_43 -> /ESP32-S3 Board/IO43
- U401 pad 50: IO_44 -> /ESP32-S3 Board/IO44
- U401 pad 51: IO_45 -> /ESP32-S3 Board/IO45
- U401 pad 52: IO_46 -> /ESP32-S3 Board/IO46
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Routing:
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- added copper zone on In3.Cu, net +3V3
- added copper zone on In4.Cu, net +5V_{FUSED}
- added copper zone on B.Cu, net +V_{BAT}
- added copper zone on F.Cu, net +V_{SW}
- added copper zone on In2.Cu, net +V_{SW}
- added copper zone on B.Cu, net /ESP32-S3 Board/USB_Power_Interface/GND1
- added copper zone on F.Cu, net /IO_Board/WLED Outputs/V_{OUT1}
- added copper zone on In2.Cu, net /IO_Board/WLED Outputs/V_{OUT1}
- added copper zone on F.Cu, net /IO_Board/WLED Outputs/V_{OUT2}
- added copper zone on In2.Cu, net /IO_Board/WLED Outputs/V_{OUT2}
- added copper zone on F.Cu, net GND2
- removed copper zone on In1.Cu, net +5V_{FUSED}
- removed copper zone on In2.Cu, net +5V_{FUSED}
- removed copper zone on In3.Cu, net +5V_{FUSED}
- removed copper zone on B.Cu, net /ESP32-S3 Board/EN/Reset
- removed copper zone on B.Cu, net /ESP32-S3 Board/IO00
- removed copper zone on B.Cu, net GND1
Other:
- board size 31 x 30.5 mm -> 31 x 63.5 mm
- board text added: "ESP32-S3 D2 Pico"
- board text removed: "ESP32-S3 Pico D1"
